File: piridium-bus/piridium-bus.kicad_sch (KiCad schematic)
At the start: 82 parts, among them J1 EPS, J2 MODEM UART, J3 INHIBITS, J4 ANT, J5 PAYLOAD, Q1 DMP3015LSSQ, Q2 Si4186DY, Q3 DMP3015LSSQ, Q4 Si4186DY, Q5 DMP3015LSSQ, Q6 DMP3015LSSQ, Q7 2N7002, Q8 DMP3015LSSQ, U1 LM1117-3.3, U2 TPS54394RSAR, U3 MAX6369, U4 74HC126, U5 INA180A3, U6 DS3232M, U7 INA180A3, U8 MCP3208

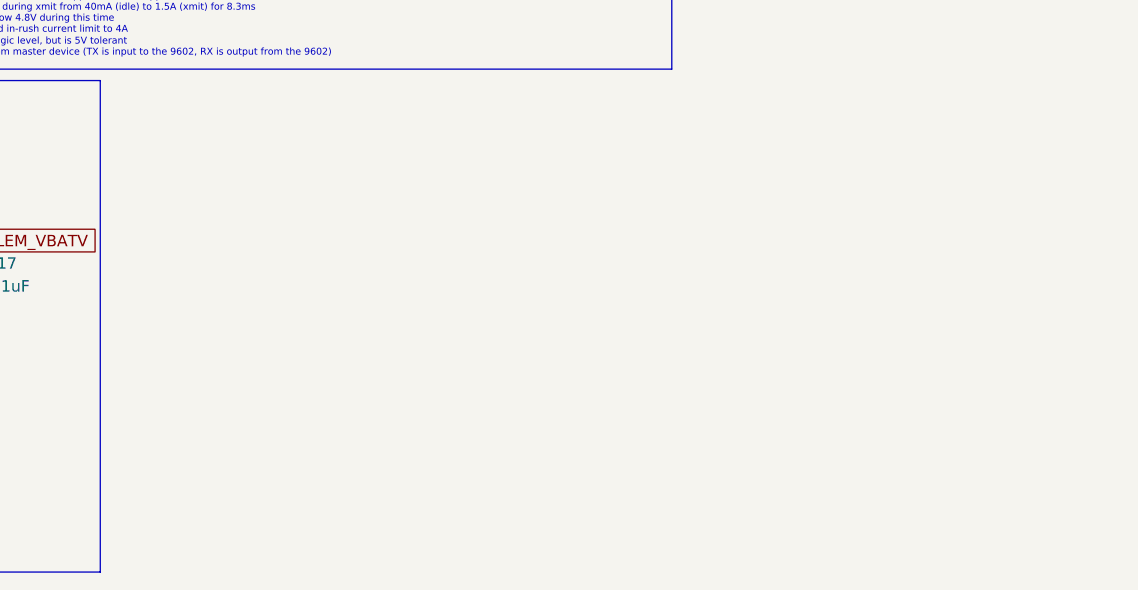
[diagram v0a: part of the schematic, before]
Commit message: add max4373f
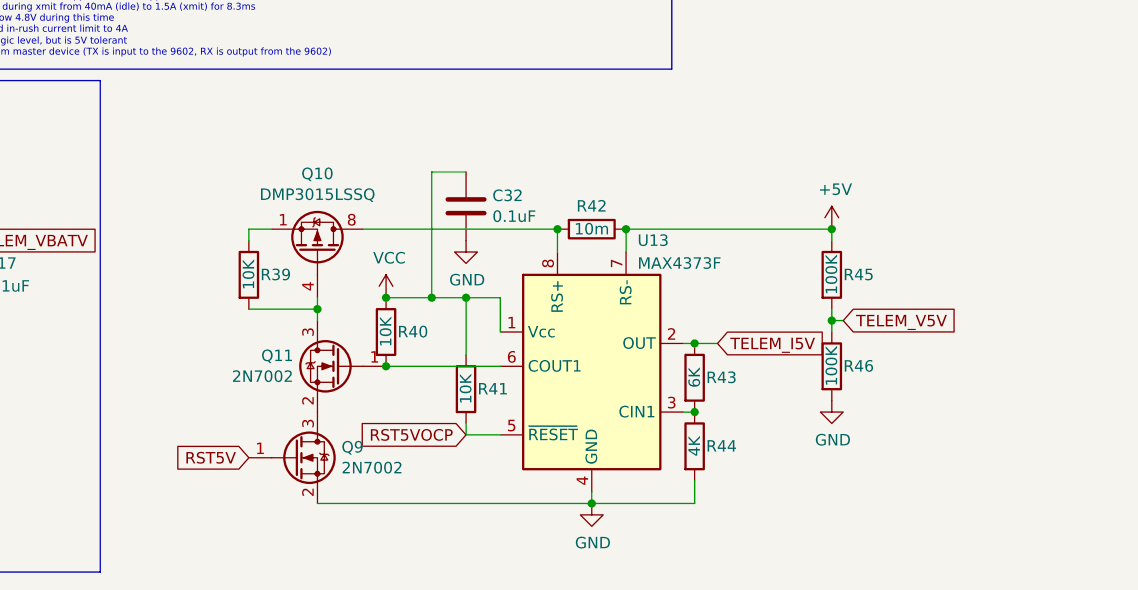
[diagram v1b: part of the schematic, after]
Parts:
- added C32: 0.1uF, Capacitor_SMD:C_0805_2012Metric, symbol Device:C
- added Q10: DMP3015LSSQ, Package_SO:SOIC-8_3.9x4.9mm_P1.27mm, symbol Transistor_FET:IRF7404
- added Q11, Q9: 2N7002, Package_TO_SOT_SMD:SOT-23, symbol Transistor_FET:2N7002
- added R39, R40, R41: 10K, Resistor_SMD:R_0805_2012Metric, symbol Device:R
- added R42: 10m, Resistor_SMD:R_1206_3216Metric, symbol Device:R
- added R43: 6K, Resistor_SMD:R_0805_2012Metric, symbol Device:R
- added R44: 4K, Resistor_SMD:R_0805_2012Metric, symbol Device:R
- added R45, R46: 100K, Resistor_SMD:R_0805_2012Metric, symbol Device:R
- added U13: MAX4373F, Package_SO:SO-8_3.9x4.9mm_P1.27mm, symbol piridium-bus:MAX4373F
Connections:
- net +5V: now also R42.1, R45.1, U13.7 (RS-)
- net GND: now also C32.2, Q9.2 (S), R44.2, R46.2, U13.4 (GND)
- new net: Q11.1 (G), R40.2, U13.6 (COUT1)
- new net: Q11.2 (S), Q9.3 (D)
- new net: Q10.4 (G), Q11.3 (D), R39.2
- new net: R43.2, R44.1, U13.3 (CIN1)
- new net: Q10.1 (S), Q10.2 (S), Q10.3 (S), R39.1
- new net: Q10.5 (D), Q10.6 (D), Q10.7 (D), Q10.8 (D), R42.2, U13.8 (RS+)
- new net RST5V: Q9.1 (G)
- new net RST5VOCP: R41.2, U13.5 (~{RESET})
- new net TELEM_I5V: R43.1, U13.2 (OUT)
- new net TELEM_V5V: R45.2, R46.1
- new net VCC: C32.1, R40.1, R41.1, U13.1 (Vcc)

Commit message: prototype timing circuit for LCL reset
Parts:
- removed Q9: 2N7002, Package_TO_SOT_SMD:SOT-23, symbol Transistor_FET:2N7002
- added C20: 10uF, Capacitor_SMD:C_0805_2012Metric, symbol Device:C
- added Q11: 2N7002, Package_TO_SOT_SMD:SOT-23, symbol Transistor_FET:2N7002
- added R26: 500K, Resistor_SMD:R_0805_2012Metric, symbol Device:R
- added U8: SN74LVC1G14DBV, Package_TO_SOT_SMD:SOT-23-5, symbol 74xGxx:SN74LVC1G14DBV
- renumbered C32 to C21, C20 to C22, C21 to C23, Q11 to Q10, Q10 to Q9, R39 to R25, R40 to R27, R41 to R28, R42 to R29, R43 to R30, R44 to R31, R45 to R32, R46 to R33, U13 to U10, U8 to U9
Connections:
- net VCC is gone; now on net +3.3VA: C21.1, R27.1, R28.1, U10.1 (Vcc)
- net GND: now also Q10.2 (S), C20.2, Q11.2 (S), U8.3 (GND)
- net at Q10.1 (G), R27.2, U10.6 (COUT1): now also U8.2
- net +3.3VA: now reaches C5.1, R8.1, U1.2 (VO), U3.4 (SET0), U3.5 (SET1), U3.6 (SET2), U3.8 (VCC)
- net +3.3VA: now also U8.5 (VCC)
- net RST5VOCP: no longer names the net of R28.2, U10.5 (~{RESET})
- net RST5VOCP: now also Q11.3 (D)
- new net: R26.1, U8.4
- new net: C20.1, Q11.1 (G), R26.2
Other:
- note added: "2n7002 Vgs(Typ) 2.1V, (max) 3V minimum reset time 5 seconds"
- note added: "Watchdog Timer, SBY 3V Rail"
- note removed: "Watchdog Timer"
- moved on the sheet: C21, Q10, Q9, R25, R27, R28, R29, R30, R31, R32, R33, U10

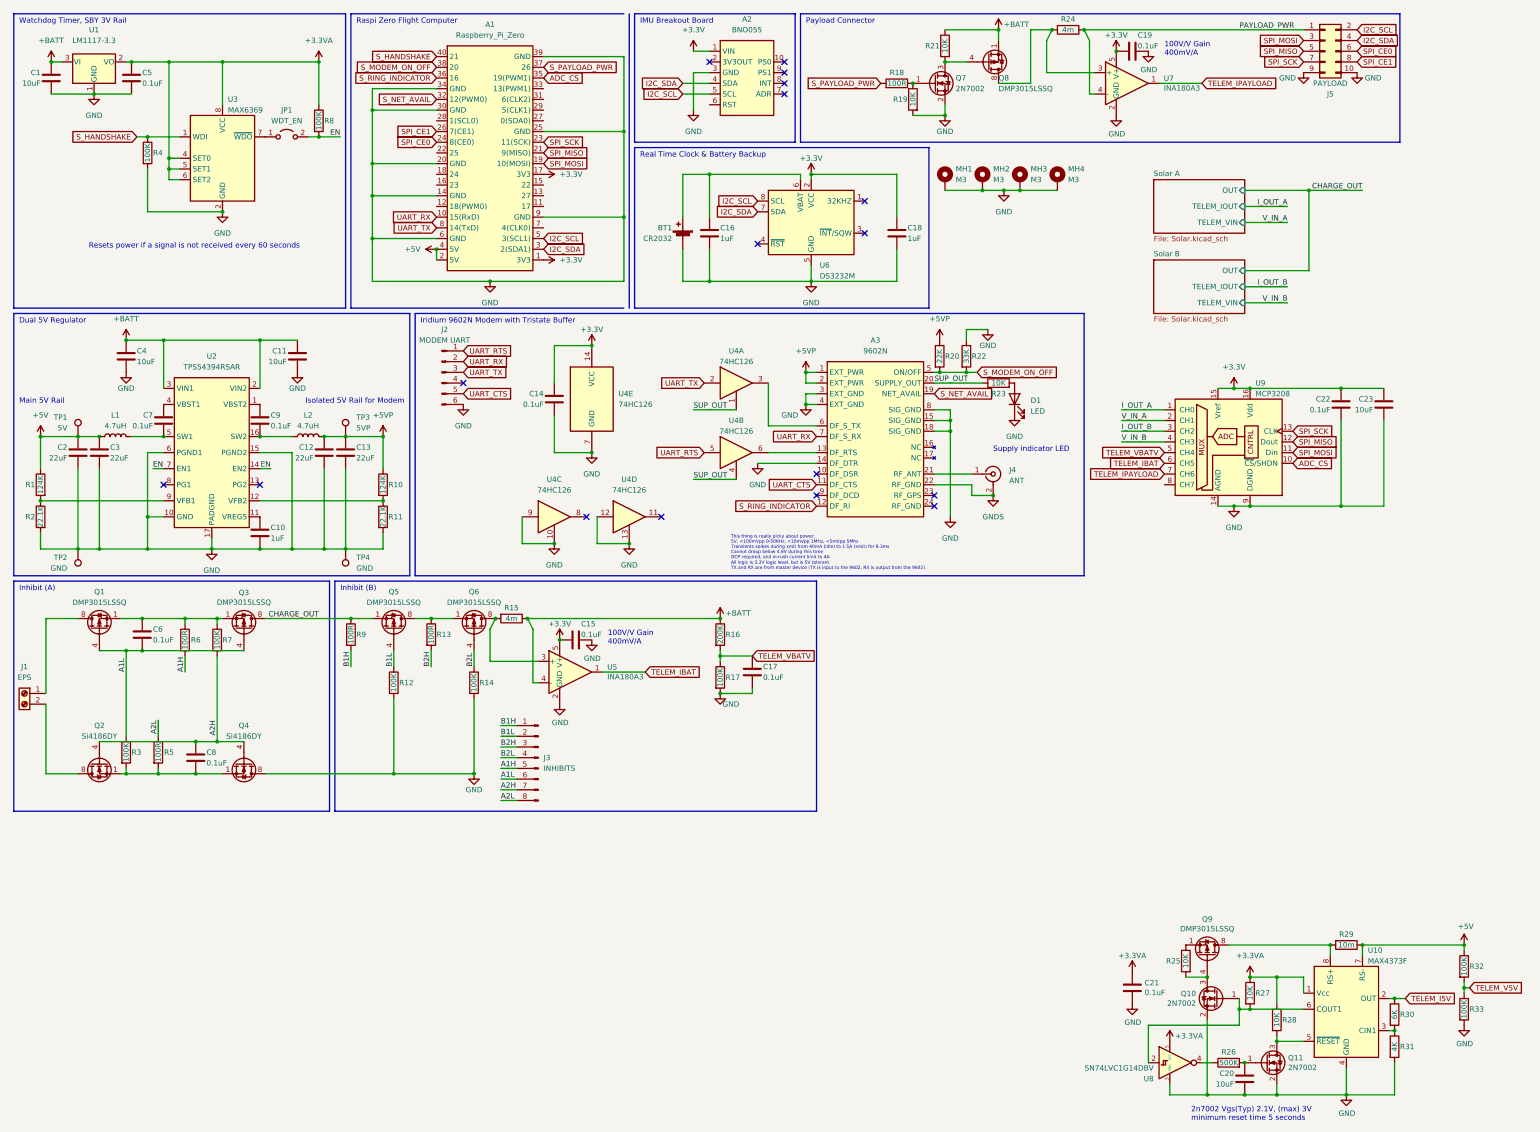
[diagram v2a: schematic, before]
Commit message: move LCLs to hierarchical sheets
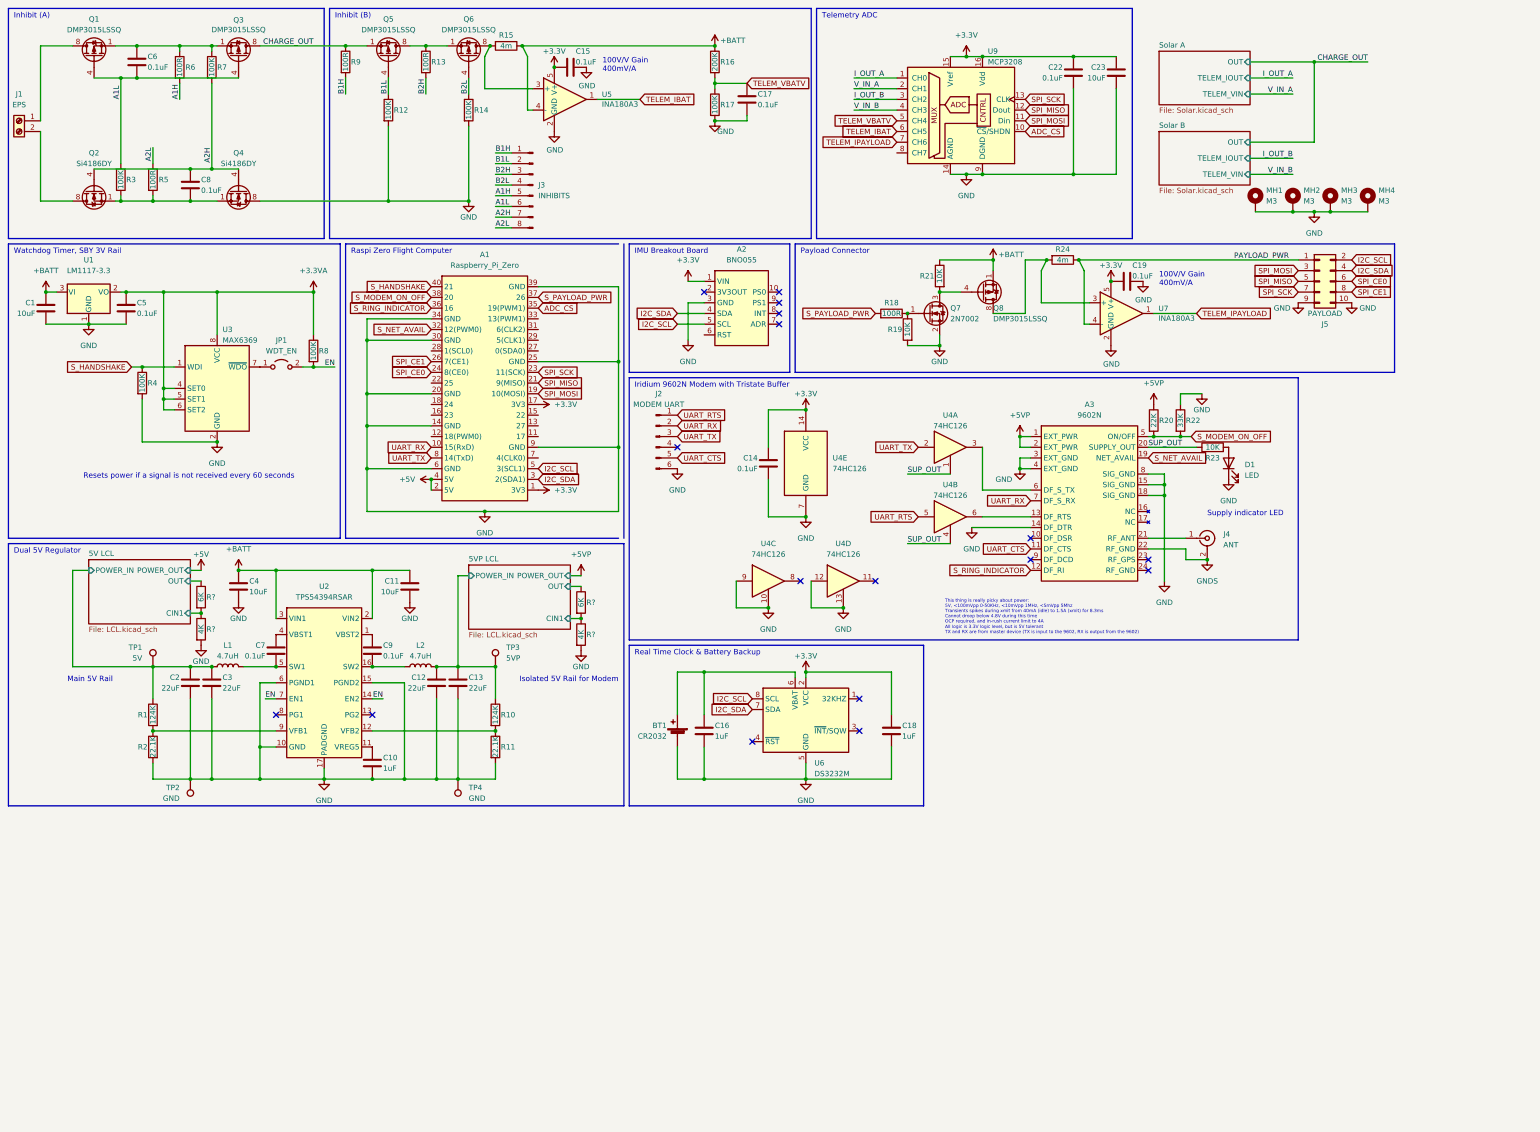
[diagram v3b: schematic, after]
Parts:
- removed C20: 10uF, Capacitor_SMD:C_0805_2012Metric, symbol Device:C
- removed C21: 0.1uF, Capacitor_SMD:C_0805_2012Metric, symbol Device:C
- removed Q10, Q11: 2N7002, Package_TO_SOT_SMD:SOT-23, symbol Transistor_FET:2N7002
- removed Q9: DMP3015LSSQ, Package_SO:SOIC-8_3.9x4.9mm_P1.27mm, symbol Transistor_FET:IRF7404
- removed R25, R27, R28: 10K, Resistor_SMD:R_0805_2012Metric, symbol Device:R
- removed R26: 500K, Resistor_SMD:R_0805_2012Metric, symbol Device:R
- removed R29: 10m, Resistor_SMD:R_1206_3216Metric, symbol Device:R
- removed R30: 6K, Resistor_SMD:R_0805_2012Metric, symbol Device:R
- removed R31: 4K, Resistor_SMD:R_0805_2012Metric, symbol Device:R
- removed R32, R33: 100K, Resistor_SMD:R_0805_2012Metric, symbol Device:R
- removed U10: MAX4373F, Package_SO:SO-8_3.9x4.9mm_P1.27mm, symbol piridium-bus:MAX4373F
- removed U8: SN74LVC1G14DBV, Package_TO_SOT_SMD:SOT-23-5, symbol 74xGxx:SN74LVC1G14DBV
- added R? (x2): 4K, Resistor_SMD:R_0805_2012Metric, symbol Device:R
- added R? (x2): 6K, Resistor_SMD:R_0805_2012Metric, symbol Device:R
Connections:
- net +5V: no longer C2.1, C3.1, L1.1, R1.1, TP1.1
- net +5VP: no longer C12.1, C13.1, L2.2, R10.1, TP3.1
- net GND: now also R?.2, R?.2
- new net 5V LCL/CIN1: R?.1, R?.2
- new net 5V LCL/OUT: R?.1
- new net 5V LCL/POWER_IN: C2.1, C3.1, L1.1, R1.1, TP1.1
- new net 5VP LCL/CIN1: R?.1, R?.2
- new net 5VP LCL/OUT: R?.1
- new net 5VP LCL/POWER_IN: C12.1, C13.1, L2.2, R10.1, TP3.1
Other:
- added sheet 5V LCL (LCL.kicad_sch)
- added sheet 5VP LCL (LCL.kicad_sch)
- note added: "Telemetry ADC"
- note removed: "2n7002 Vgs(Typ) 2.1V, (max) 3V minimum reset time 5 seconds"
- moved on the sheet: A1, A2, A3, BT1, C1, C10, C11, C12, C13, C14, C15, C16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

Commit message: battery sch finish
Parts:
- gave numbers to parts that had none: 4
- renumbered C15 to C14, C16 to C15, C17 to C16, C14 to C17, C22 to C19, C5 to C2, C23 to C20, C19 to C21, C6 to C3, C8 to C4, C2 to C5, C3 to C6, C4 to C7, C7 to C8, J3 to J2, J2 to J3, R3 to R1, R8 to R10, R9 to R11, R10 to R15, R11 to R16, R15 to R17, R4 to R2, R16 to R20, R17 to R21, R18 to R22, R19 to R23, R21 to R24, R24 to R25, R20 to R26, R22 to R27, R23 to R28, R5 to R3, R1 to R4, R2 to R5, R7 to R9, TP4 to TP3, TP3 to TP4, U3 to U2, U2 to U3, U5 to U4, U4 to U5, U9 to U7, U7 to U8

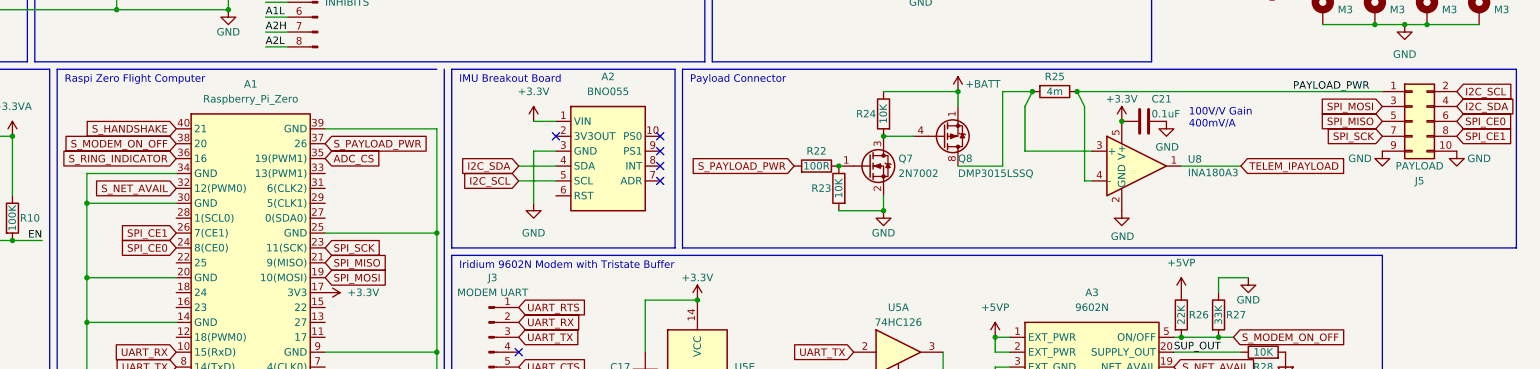
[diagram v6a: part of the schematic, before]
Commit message: move adc to hardware cs pin, start routing updated LCLs
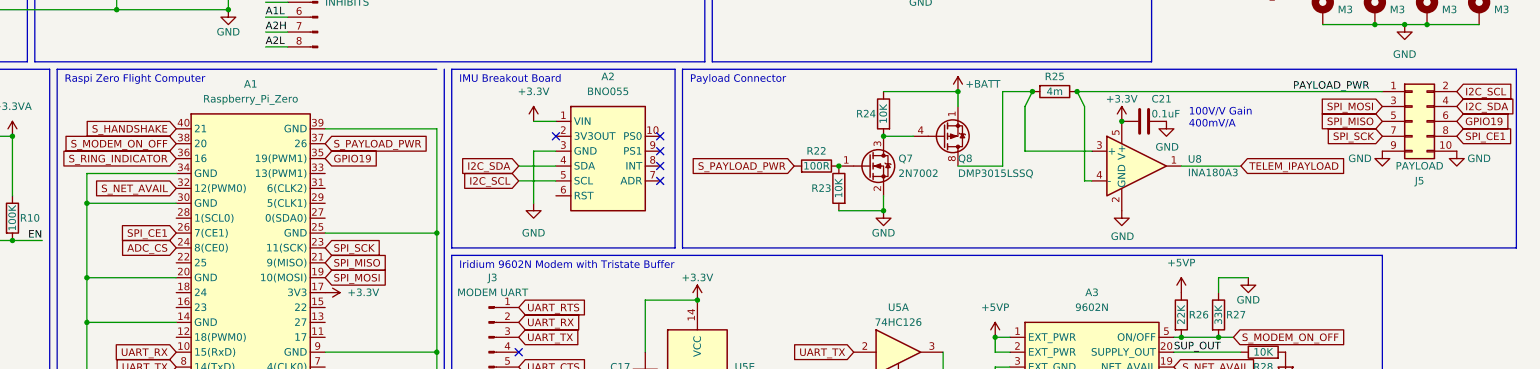
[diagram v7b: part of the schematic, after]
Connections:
- net ADC_CS: now also A1.24 (8(CE0)); no longer A1.35 (19(PWM1))
- net SPI_CE0 renamed GPIO19
- net GPIO19: now also A1.35 (19(PWM1)); no longer A1.24 (8(CE0))
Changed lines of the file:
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@@
-    )
-  )
-  (global_label "SPI_CE0" (shape input) (at 113.03 99.06 180) (fields_autoplaced)
-    (effects (font (size 1.27 1.27)) (justify right))
-    (property "Intersheet References" "${INTERSHEET_REFS}" (id 0) (at 102.9364 98.9806 0)
-      (effects (font (size 1.27 1.27)) (justify right) hide)
     )
   )
@@
     )
   )
-  (global_label "ADC_CS" (shape input) (at 138.43 83.82 0) (fields_autoplaced)
-    (effects (font (size 1.27 1.27)) (justify left))
-    (property "Intersheet References" "${INTERSHEET_REFS}" (id 0) (at 147.9188 83.7406 0)
-      (effects (font (size 1.27 1.27)) (justify left) hide)
+  (global_label "ADC_CS" (shape input) (at 113.03 99.06 180) (fields_autoplaced)
+    (effects (font (size 1.27 1.27)) (justify right))
+    (property "Intersheet References" "${INTERSHEET_REFS}" (id 0) (at 103.5412 99.1394 0)
+      (effects (font (size 1.27 1.27)) (justify right) hide)
     )
   )
@@
     )
   )
+  (global_label "GPIO19" (shape input) (at 138.43 83.82 0) (fields_autoplaced)
+    (effects (font (size 1.27 1.27)) (justify left))
+    (property "Intersheet References" "${INTERSHEET_REFS}" (id 0) (at 147.7374 83.7406 0)
+      (effects (font (size 1.27 1.27)) (justify left) hide)
+    )
+  )
   (global_label "SPI_MISO" (shape input) (at 138.43 101.6 0) (fields_autoplaced)
     (effects (font (size 1.27 1.27)) (justify left))
@@
     )
   )
+  (global_label "GPIO19" (shape input) (at 331.47 77.47 0) (fields_autoplaced)
+    (effects (font (size 1.27 1.27)) (justify left))
+    (property "Intersheet References" "${INTERSHEET_REFS}" (id 0) (at 340.7774 77.3906 0)
+      (effects (font (size 1.27 1.27)) (justify left) hide)
+    )
+  )
   (global_label "S_MODEM_ON_OFF" (shape input) (at 113.03 81.28 180) (fields_autoplaced)
     (effects (font (size 1.27 1.27)) (justify right))
@@
     )
   )
-  (global_label "SPI_CE0" (shape input) (at 331.47 77.47 0) (fields_autoplaced)
-    (effects (font (size 1.27 1.27)) (justify left))
-    (property "Intersheet References" "${INTERSHEET_REFS}" (id 0) (at 341.5636 77.5494 0)
-      (effects (font (size 1.27 1.27)) (justify left) hide)
-    )
-  )
